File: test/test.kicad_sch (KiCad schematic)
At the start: 2 parts

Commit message: added 2 footprints
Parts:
- DE: footprint (none) -> LED_SMD:LED_01005_0402Metric
- REEFF: footprint (none) -> Resistor_SMD:R_01005_0402Metric
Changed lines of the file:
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@@
 			)
 		)
-		(property "Footprint" ""
+		(property "Footprint" "LED_SMD:LED_01005_0402Metric"
 			(at 105.41 114.3 0)
 			(hide yes)
@@
 			)
 		)
-		(property "Footprint" ""
+		(property "Footprint" "Resistor_SMD:R_01005_0402Metric"
 			(at 52.832 114.3 90)
 			(hide yes)

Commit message: cleaned kicad
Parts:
- removed DE: LEEED, LED_SMD:LED_01005_0402Metric, symbol Device:LED
- removed REEFF: R, Resistor_SMD:R_01005_0402Metric, symbol Device:R
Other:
- company: firma  -> (none)
- title: Titelll ! -> (none)

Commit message: Symbol added (ref and val changed) wire added, title till comment 1 added
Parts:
- added ResRef: ResVal1, symbol Device:R
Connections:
- new net: ResRef.1, ResRef.2
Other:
- company: (none) -> SELAB
- title: (none) -> TestBoard
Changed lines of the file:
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@@
 	(generator_version "10.0")
 	(paper "A4")
+	(title_block
+		(title "TestBoard")
+		(date "2026-07-03")
+		(rev "v1")
+		(company "SELAB")
+		(comment 1 "Wichtige Sachen")
+	)
+	(wire
+		(pts
+			(xy 99.06 88.9) (xy 99.06 92.71)
+		)
+		(stroke
+			(width 0)
+			(type default)
+		)
+	)
+	(wire
+		(pts
+			(xy 99.06 101.6) (xy 114.3 101.6)
+		)
+		(stroke
+			(width 0)
+			(type default)
+		)
+	)
+	(wire
+		(pts
+			(xy 114.3 101.6) (xy 114.3 88.9)
+		)
+		(stroke
+			(width 0)
+			(type default)
+		)
+	)
+	(wire
+		(pts
+			(xy 114.3 88.9) (xy 99.06 88.9)
+		)
+		(stroke
+			(width 0)
+			(type default)
+		)
+	)
+	(wire
+		(pts
+			(xy 99.06 100.33) (xy 99.06 101.6)
+		)
+		(stroke
+			(width 0)
+			(type default)
+		)
+	)
+	(symbol
+		(lib_id "Device:R")
+		(at 99.06 96.52 0)
+		(unit 1)
+		(body_style 1)
+		(exclude_from_sim no)
+		(in_bom yes)
+		(on_board yes)
+		(in_pos_files yes)
+		(dnp no)
+		(fields_autoplaced yes)
+		(property "Reference" "ResRef"
+			(at 101.6 95.2499 0)
+			(show_name no)
+			(do_not_autoplace no)
+			(effects
+				(font
+					(size 1.27 1.27)
+				)
+				(justify left)
+			)
+		)
+		(property "Value" "ResVal1"
+			(at 101.6 97.7899 0)
+			(show_name no)
+			(do_not_autoplace no)
+			(effects
+				(font
+					(size 1.27 1.27)
+				)
+				(justify left)
+			)
+		)
+		(property "Footprint" ""
+			(at 97.282 96.52 90)
+			(hide yes)
+			(show_name no)
+			(do_not_autoplace no)
+			(effects
+				(font
+					(size 1.27 1.27)
+				)
+			)
+		)
+		(property "Datasheet" ""
+			(at 99.06 96.52 0)
+			(hide yes)
+			(show_name no)
+			(do_not_autoplace no)
+			(effects
+				(font
+					(size 1.27 1.27)
+				)
+			)
+		)
+		(property "Description" "Resistor"
+			(at 99.06 96.52 0)
+			(hide yes)
+			(show_name no)
+			(do_not_autoplace no)
+			(effects
+				(font
+					(size 1.27 1.27)
+				)
+			)
+		)
+		(pin "1"
+		)
+		(pin "2"
+		)
+		(instances
+			(project "test"
+				(path "/2fe60de8-5e34-47a1-855a-3a2b581508e8"
+					(reference "ResRef")
+					(unit 1)
+				)
+			)
+		)
+	)
 	(sheet_instances
 		(path "/"

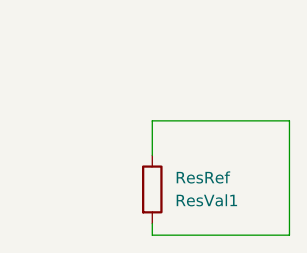
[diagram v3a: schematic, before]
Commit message: Symbol moved rotated ref val  footprint added status desc wire moved title updated
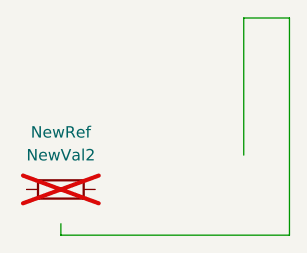
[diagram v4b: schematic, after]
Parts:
- NewRef: renamed from ResRef; value ResVal1 -> NewVal2; footprint (none) -> LED_SMD:LED_01005_0402Metric; now not fitted; now left out of the parts list
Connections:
- net at NewRef.1: no longer NewRef.2
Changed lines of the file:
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@@
 	(title_block
 		(title "TestBoard")
-		(date "2026-07-03")
-		(rev "v1")
+		(date "2026-07-04")
+		(rev "v2")
 		(company "SELAB")
 		(comment 1 "Wichtige Sachen")
+		(comment 2 "Noch wichtiger ")
+		(comment 6 "am wichtigsten")
 	)
 	(wire
 		(pts
-			(xy 99.06 88.9) (xy 99.06 92.71)
+			(xy 109.22 77.47) (xy 109.22 92.71)
 		)
 		(stroke
@@
 	(wire
 		(pts
-			(xy 99.06 101.6) (xy 114.3 101.6)
+			(xy 88.9 101.6) (xy 114.3 101.6)
 		)
 		(stroke
@@
 	(wire
 		(pts
-			(xy 114.3 101.6) (xy 114.3 88.9)
+			(xy 114.3 101.6) (xy 114.3 77.47)
 		)
 		(stroke
@@
 	(wire
 		(pts
-			(xy 114.3 88.9) (xy 99.06 88.9)
+			(xy 114.3 77.47) (xy 109.22 77.47)
 		)
 		(stroke
@@
 	(wire
 		(pts
-			(xy 99.06 100.33) (xy 99.06 101.6)
+			(xy 88.9 100.33) (xy 88.9 101.6)
 		)
 		(stroke
@@
 	(symbol
 		(lib_id "Device:R")
-		(at 99.06 96.52 0)
+		(at 88.9 96.52 270)
 		(unit 1)
 		(body_style 1)
 		(exclude_from_sim no)
-		(in_bom yes)
-		(on_board yes)
+		(in_bom no)
+		(on_board no)
 		(in_pos_files yes)
-		(dnp no)
+		(dnp yes)
 		(fields_autoplaced yes)
-		(property "Reference" "ResRef"
-			(at 101.6 95.2499 0)
+		(property "Reference" "NewRef"
+			(at 88.9 90.17 90)
 			(show_name no)
 			(do_not_autoplace no)
@@
 					(size 1.27 1.27)
 				)
-				(justify left)
 			)
 		)
-		(property "Value" "ResVal1"
-			(at 101.6 97.7899 0)
+		(property "Value" "NewVal2"
+			(at 88.9 92.71 90)
 			(show_name no)
 			(do_not_autoplace no)
@@
 					(size 1.27 1.27)
 				)
-				(justify left)
 			)
 		)
-		(property "Footprint" ""
-			(at 97.282 96.52 90)
+		(property "Footprint" "LED_SMD:LED_01005_0402Metric"
+			(at 88.9 94.742 90)
 			(hide yes)
 			(show_name no)
@@
 		)
 		(property "Datasheet" ""
-			(at 99.06 96.52 0)
+			(at 88.9 96.52 0)
 			(hide yes)
 			(show_name no)
@@
 			)
 		)
-		(property "Description" "Resistor"
-			(at 99.06 96.52 0)
+		(property "Description" "This is a Resistor"
+			(at 88.9 96.52 0)
 			(hide yes)
 			(show_name no)
@@
 			(project "test"
 				(path "/2fe60de8-5e34-47a1-855a-3a2b581508e8"
-					(reference "ResRef")
+					(reference "NewRef")
 					(unit 1)
 				)

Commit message: footprint changed
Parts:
- NewRef: footprint LED_SMD:LED_01005_0402Metric -> Resistor_SMD:R_0603_1608Metric
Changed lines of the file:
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@@
 			)
 		)
-		(property "Footprint" "LED_SMD:LED_01005_0402Metric"
+		(property "Footprint" "Resistor_SMD:R_0603_1608Metric"
 			(at 88.9 94.742 90)
 			(hide yes)

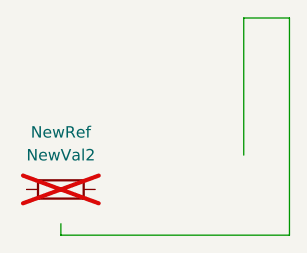
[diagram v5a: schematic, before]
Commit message: Deleted wire removed footprints and status removed all info from title
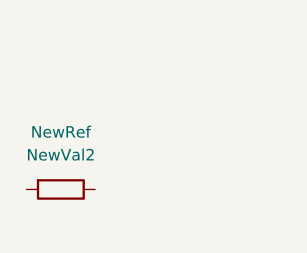
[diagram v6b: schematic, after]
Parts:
- NewRef: footprint Resistor_SMD:R_0603_1608Metric -> (none); now fitted; now in the parts list
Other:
- company: SELAB -> (none)
- title: TestBoard -> (none)
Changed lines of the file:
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@@
 	(generator_version "10.0")
 	(paper "A4")
-	(title_block
-		(title "TestBoard")
-		(date "2026-07-04")
-		(rev "v2")
-		(company "SELAB")
-		(comment 1 "Wichtige Sachen")
-		(comment 2 "Noch wichtiger ")
-		(comment 6 "am wichtigsten")
-	)
-	(wire
-		(pts
-			(xy 109.22 77.47) (xy 109.22 92.71)
-		)
-		(stroke
-			(width 0)
-			(type default)
-		)
-	)
-	(wire
-		(pts
-			(xy 88.9 101.6) (xy 114.3 101.6)
-		)
-		(stroke
-			(width 0)
-			(type default)
-		)
-	)
-	(wire
-		(pts
-			(xy 114.3 101.6) (xy 114.3 77.47)
-		)
-		(stroke
-			(width 0)
-			(type default)
-		)
-	)
-	(wire
-		(pts
-			(xy 114.3 77.47) (xy 109.22 77.47)
-		)
-		(stroke
-			(width 0)
-			(type default)
-		)
-	)
-	(wire
-		(pts
-			(xy 88.9 100.33) (xy 88.9 101.6)
-		)
-		(stroke
-			(width 0)
-			(type default)
-		)
-	)
 	(symbol
 		(lib_id "Device:R")
@@
 		(body_style 1)
 		(exclude_from_sim no)
-		(in_bom no)
-		(on_board no)
+		(in_bom yes)
+		(on_board yes)
 		(in_pos_files yes)
-		(dnp yes)
+		(dnp no)
 		(fields_autoplaced yes)
 		(property "Reference" "NewRef"
@@
 			)
 		)
-		(property "Footprint" "Resistor_SMD:R_0603_1608Metric"
+		(property "Footprint" ""
 			(at 88.9 94.742 90)
 			(hide yes)

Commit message: removed symbol
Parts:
- removed NewRef: NewVal2, symbol Device:R
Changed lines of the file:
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@@
 	(generator_version "10.0")
 	(paper "A4")
-	(symbol
-		(lib_id "Device:R")
-		(at 88.9 96.52 270)
-		(unit 1)
-		(body_style 1)
-		(exclude_from_sim no)
-		(in_bom yes)
-		(on_board yes)
-		(in_pos_files yes)
-		(dnp no)
-		(fields_autoplaced yes)
-		(property "Reference" "NewRef"
-			(at 88.9 90.17 90)
-			(show_name no)
-			(do_not_autoplace no)
-			(effects
-				(font
-					(size 1.27 1.27)
-				)
-			)
-		)
-		(property "Value" "NewVal2"
-			(at 88.9 92.71 90)
-			(show_name no)
-			(do_not_autoplace no)
-			(effects
-				(font
-					(size 1.27 1.27)
-				)
-			)
-		)
-		(property "Footprint" ""
-			(at 88.9 94.742 90)
-			(hide yes)
-			(show_name no)
-			(do_not_autoplace no)
-			(effects
-				(font
-					(size 1.27 1.27)
-				)
-			)
-		)
-		(property "Datasheet" ""
-			(at 88.9 96.52 0)
-			(hide yes)
-			(show_name no)
-			(do_not_autoplace no)
-			(effects
-				(font
-					(size 1.27 1.27)
-				)
-			)
-		)
-		(property "Description" "This is a Resistor"
-			(at 88.9 96.52 0)
-			(hide yes)
-			(show_name no)
-			(do_not_autoplace no)
-			(effects
-				(font
-					(size 1.27 1.27)
-				)
-			)
-		)
-		(pin "1"
-		)
-		(pin "2"
-		)
-		(instances
-			(project "test"
-				(path "/2fe60de8-5e34-47a1-855a-3a2b581508e8"
-					(reference "NewRef")
-					(unit 1)
-				)
-			)
-		)
-	)
 	(sheet_instances
 		(path "/"

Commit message: 3 sym 3 wire 3 ft title added
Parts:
- added D1: LED, LED_SMD:LED_01005_0402Metric, symbol Device:LED
- added R1: R, Resistor_SMD:R_01005_0402Metric, symbol Device:R
- added U1: CHIP-PRO, Module:MODULE_NEXTTHINGCO_CHIPPRO, symbol MCU_Module:CHIP-PRO
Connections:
- new net: R1.2, U1.18 (HPL)
- new net: U1.21 (PB5/I2S-MCLK), U1.5 (~{POWER-ON})
- new net: D1.2 (A), U1.51 (USB0-D+)
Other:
- company: (none) -> SELAB INC
- title: (none) -> BestBoard
